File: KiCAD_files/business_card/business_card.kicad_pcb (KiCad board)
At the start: 2 copper layers, 88.9 x 50.8 mm, 114 parts, among them J2 Conn_01x05_Pin, Q1 AO3401A, SW1 CS1210F260, SW2 CS1210F260, SW3 CS1210F260, U1 STM32U073CCUx, U2 ST25DV04KC-IE6S3

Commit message: Add NFC Antenna
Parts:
- removed C2: 100nF, Capacitor_SMD:C_0603_1608Metric
- removed R10, R9: 10K, Resistor_SMD:R_0603_1608Metric
- added L1: 2.755 uH, Antenna:25X48MM_NFC, F.Cu at (164.4, 72.8)
- U2: value ST25DV04KC-IE6S3 -> ST25TN01K-AFH5; footprint ST25DV04KC-IE6S3:SO-8_STM -> ST25TN01K-AFH5:UFDFPN-5_1P8X1P5_STM
- moved G*** 57.5 mm to (120.2, 32.6)
- moved U2 9.94 mm to (147.2, 73.0), turned to 90 degrees
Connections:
- U1 pad 16: /NFC_SDA -> unconnected-(U1-PA6-Pad16)
- U1 pad 17: /NFC_SCL -> unconnected-(U1-PA7-Pad17)
- U2 pad 2: /L = 5.634 uH -> unconnected-(U2-NC-Pad2)
- U2 pad 3: /L = 5.634 uH -> Net-(U2-AC0)
- U2 pad 4: GND -> Net-(U2-AC1)
- U2 pad 5: /NFC_SDA -> unconnected-(U2-NC-Pad5)
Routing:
- net Net-(BT1-+): track 483.6 -> 11.7 mm
- net VDD: track 126.5 -> 105.1 mm, vias 4 -> 2
- net /NFC_SCL: track 12.4 -> 0.00 mm
- net /NFC_SDA: track 11.5 -> 0.00 mm, vias 2 -> 0
- net GND: track 101.3 -> 90.1 mm, vias 16 -> 14
- net Net-(U2-AC1): track 0.00 -> 7.45 mm, vias 0 -> 1
- net Net-(U2-AC0): track 0.00 -> 3.44 mm

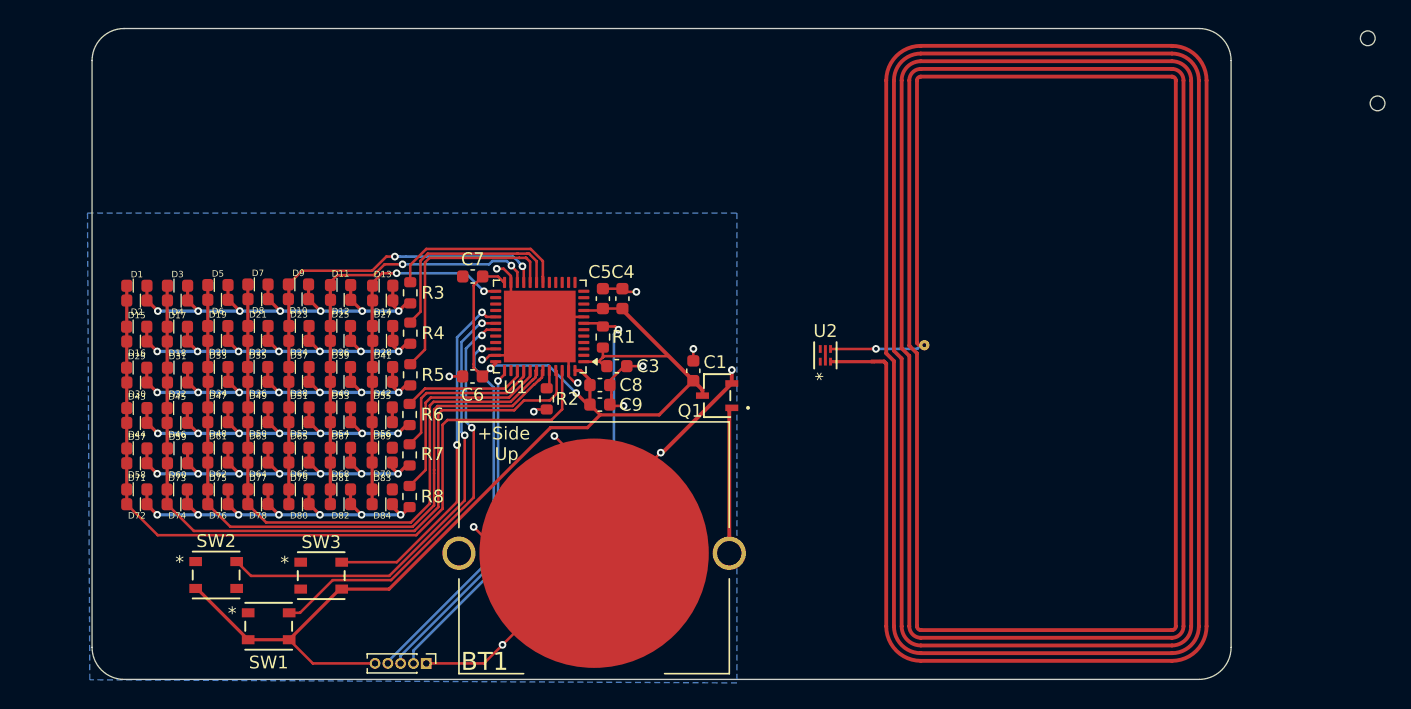
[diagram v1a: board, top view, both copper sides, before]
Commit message: Adjust LED Matrix Size
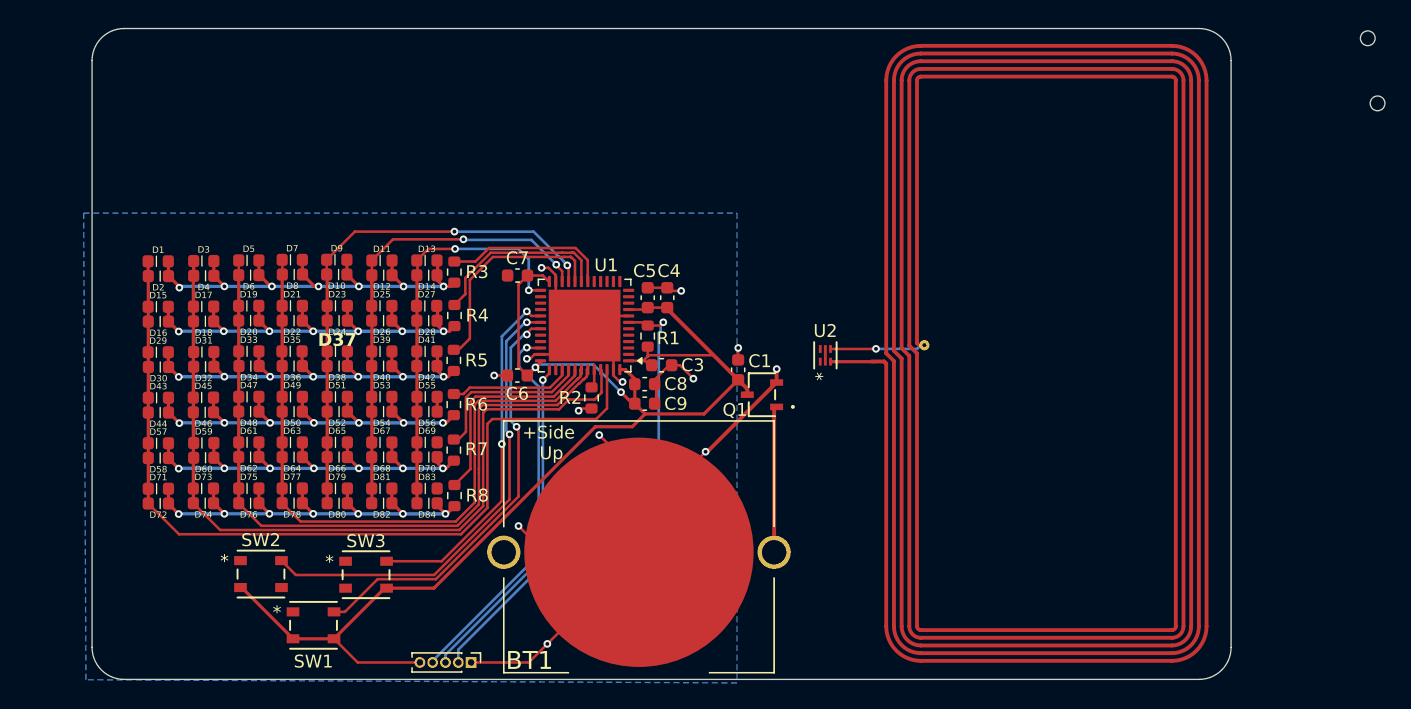
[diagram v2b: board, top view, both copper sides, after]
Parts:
- moved D13 3.97 mm to (116.0, 65.6)
- moved D14 3.97 mm to (116.0, 66.8)
- moved R3 3.80 mm to (118.2, 66.5)
- moved D27 3.78 mm to (116.0, 69.1)
- moved D28 3.78 mm to (116.0, 70.3)
- moved D11 3.76 mm to (112.5, 65.6)
- moved D12 3.76 mm to (112.5, 66.8)
- moved R4 3.71 mm to (118.2, 69.9)
- moved D41 3.67 mm to (116.0, 72.7)
- moved D42 3.67 mm to (116.0, 73.8)
- moved D55 3.60 mm to (116.1, 76.2)
- moved D56 3.60 mm to (116.1, 77.4)
- moved D25 3.59 mm to (112.5, 69.1)
- moved D26 3.59 mm to (112.5, 70.3)
- moved R5 3.58 mm to (118.2, 73.4)
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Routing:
- net /COL7: track 27.8 -> 32.1 mm
- net /COL1: track 63.0 -> 66.3 mm
- net /COL2: track 58.9 -> 62.0 mm
- net /COL5: track 38.2 -> 41.2 mm
- net /COL6: track 33.8 -> 36.6 mm
- net /COL3: track 53.7 -> 56.4 mm
- net /COL4: track 50.0 -> 52.4 mm
- net /ROW2: track 16.3 -> 14.2 mm
- net Net-(D1-A): track 36.6 -> 38.5 mm
- net Net-(D71-A): track 35.1 -> 36.9 mm
- net Net-(D43-A): track 35.4 -> 37.2 mm
- net Net-(D57-A): track 35.3 -> 37.0 mm
- net Net-(D15-A): track 36.1 -> 37.8 mm
- net /ROW3: track 18.5 -> 16.8 mm
- net Net-(D29-A): track 36.1 -> 37.8 mm
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
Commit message: Add Mouse Bites to Isolate Tooling Holes
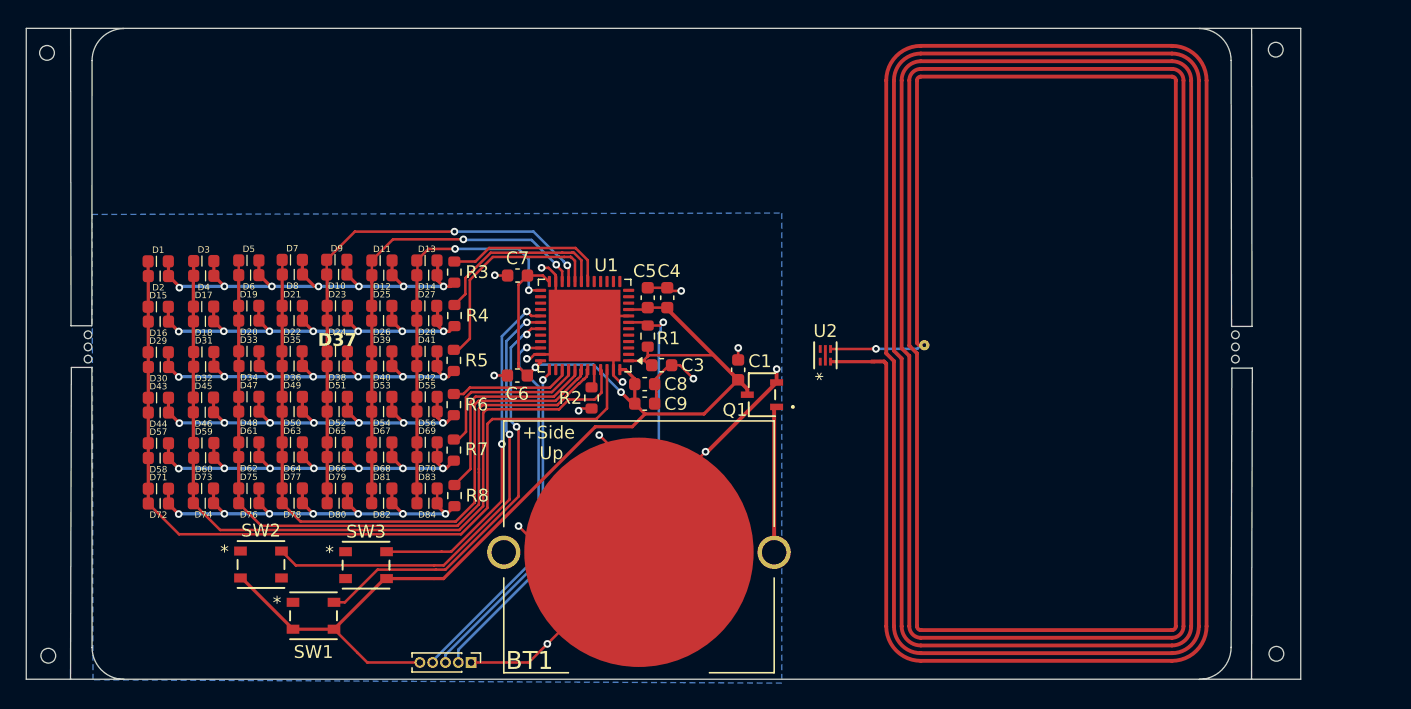
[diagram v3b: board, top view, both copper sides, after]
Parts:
- added H3: MountingHole, MountingHole:ToolingHole_1.152mm, F.Cu at (182.3, 49.1)
- added H4: MountingHole, MountingHole:ToolingHole_1.152mm, F.Cu at (86.5, 96.5)
- moved H2 103.1 mm to (86.4, 49.4)
- moved H1 43.7 mm to (182.3, 96.3)
- moved SW1 0.75 mm to (107.2, 93.3)
- moved SW2 0.75 mm to (103.1, 89.3)
- moved SW3 0.75 mm to (111.3, 89.4)
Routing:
- net Net-(D71-A): track 36.9 -> 38.0 mm
- net Net-(D57-A): track 37.0 -> 38.2 mm
- net Net-(D43-A): track 37.2 -> 38.3 mm
- net GND: track 90.0 -> 91.0 mm, vias 13 -> 14
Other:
- board size 88.9 x 50.8 mm -> 99.5 x 50.8 mm

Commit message: Move Components and Remove Unnecessary Silkscreen
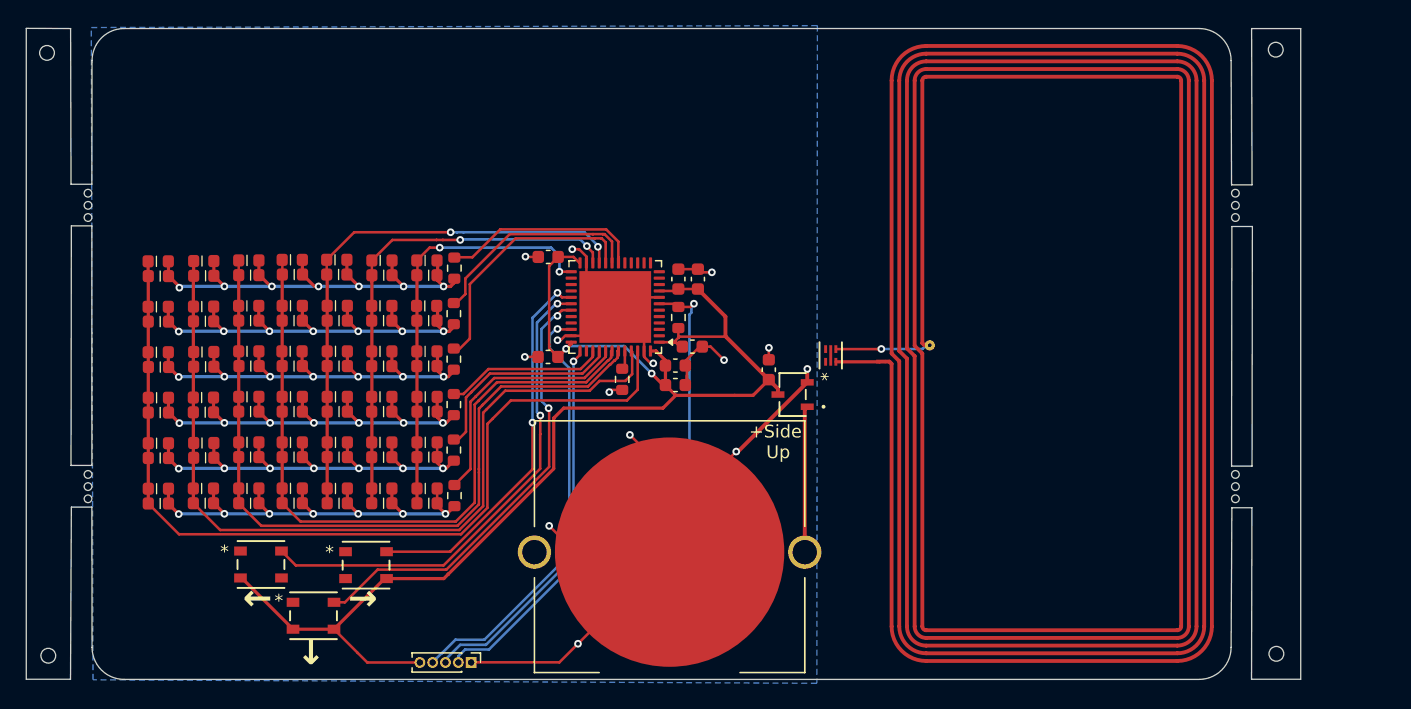
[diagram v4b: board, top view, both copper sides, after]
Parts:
- removed G***: LOGO, custom_footprints:qr_code
- moved C3 2.80 mm to (136.8, 72.3)
- moved C4 2.80 mm to (137.2, 67.1)
- moved C5 2.80 mm to (135.7, 67.1)
- moved C6 2.80 mm to (125.5, 73.1)
- moved C7 2.80 mm to (125.5, 65.3)
- moved C8 2.80 mm to (135.4, 73.8)
- moved C9 2.80 mm to (135.4, 75.3)
- moved R1 2.80 mm to (135.7, 70.1)
- moved R2 2.80 mm to (131.3, 74.9)
- moved U1 2.80 mm to (130.8, 69.2)
- moved C1 2.39 mm to (142.7, 74.1)
- moved Q1 2.39 mm to (144.6, 76.1)
- moved BT1 2.39 mm to (135.0, 88.4)
- moved L1 0.42 mm to (164.8, 72.9)
- moved U2 0.42 mm to (147.6, 73.0)
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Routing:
- net /SWDIO: track 30.0 -> 33.9 mm
- net /SWCLK: track 26.2 -> 29.8 mm
- net /NRST: track 36.1 -> 39.6 mm
- net /COL1: track 66.3 -> 69.3 mm
- net /ROW6: track 16.5 -> 19.5 mm
- net /ROW5: track 13.1 -> 16.0 mm
- net /COL3: track 56.4 -> 59.4 mm
- net /ROW4: track 9.51 -> 12.5 mm
- net /COL4: track 52.4 -> 55.4 mm
- net /COL2: track 62.0 -> 64.9 mm
- net /ROW2: track 14.2 -> 17.2 mm
- net /ROW1: track 12.9 -> 15.8 mm
- net /ROW3: track 16.8 -> 19.6 mm
- net /INPUT_DOWN: track 32.7 -> 35.2 mm
- net /INPUT_LEFT: track 36.1 -> 38.6 mm
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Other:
- outline, holes or cut-outs redrawn
- board text added: "←"
- board text added: "→"
- board text added: "↓"

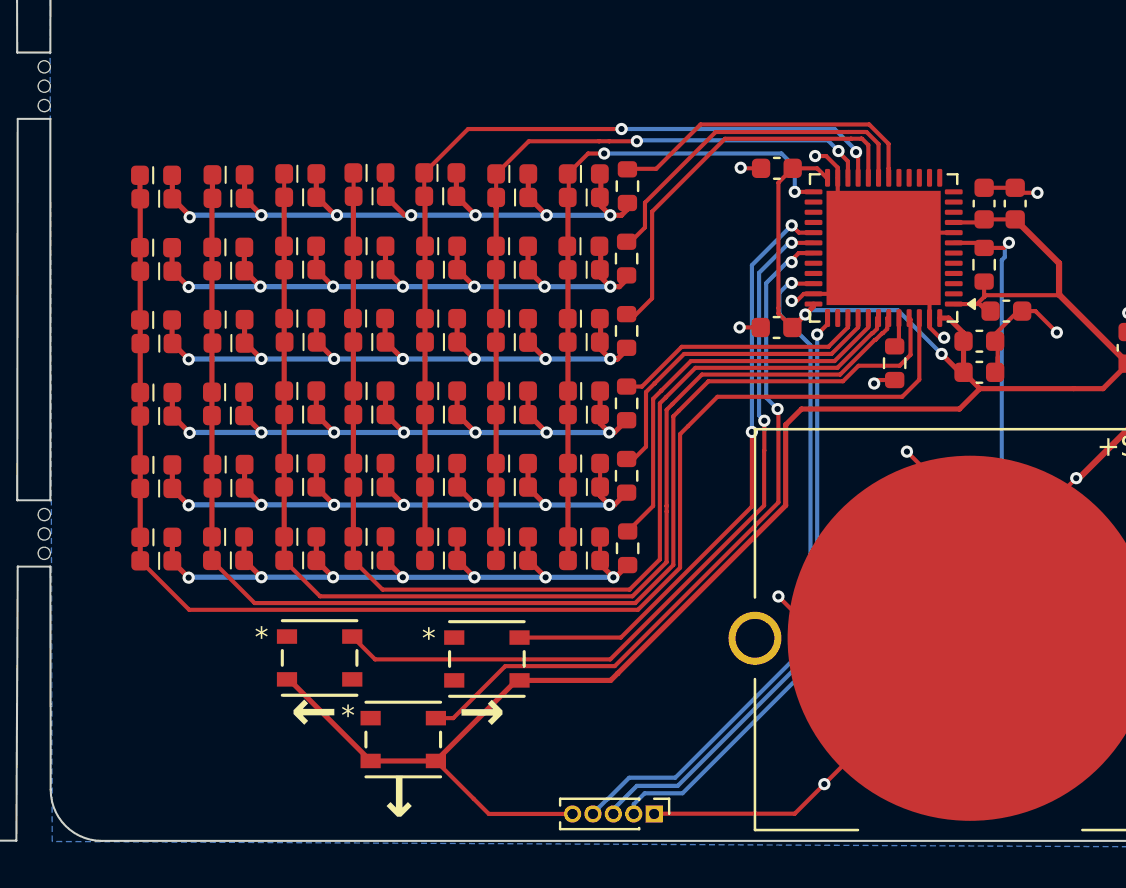
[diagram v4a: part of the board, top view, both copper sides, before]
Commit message: Change Debug Interface Connector Size
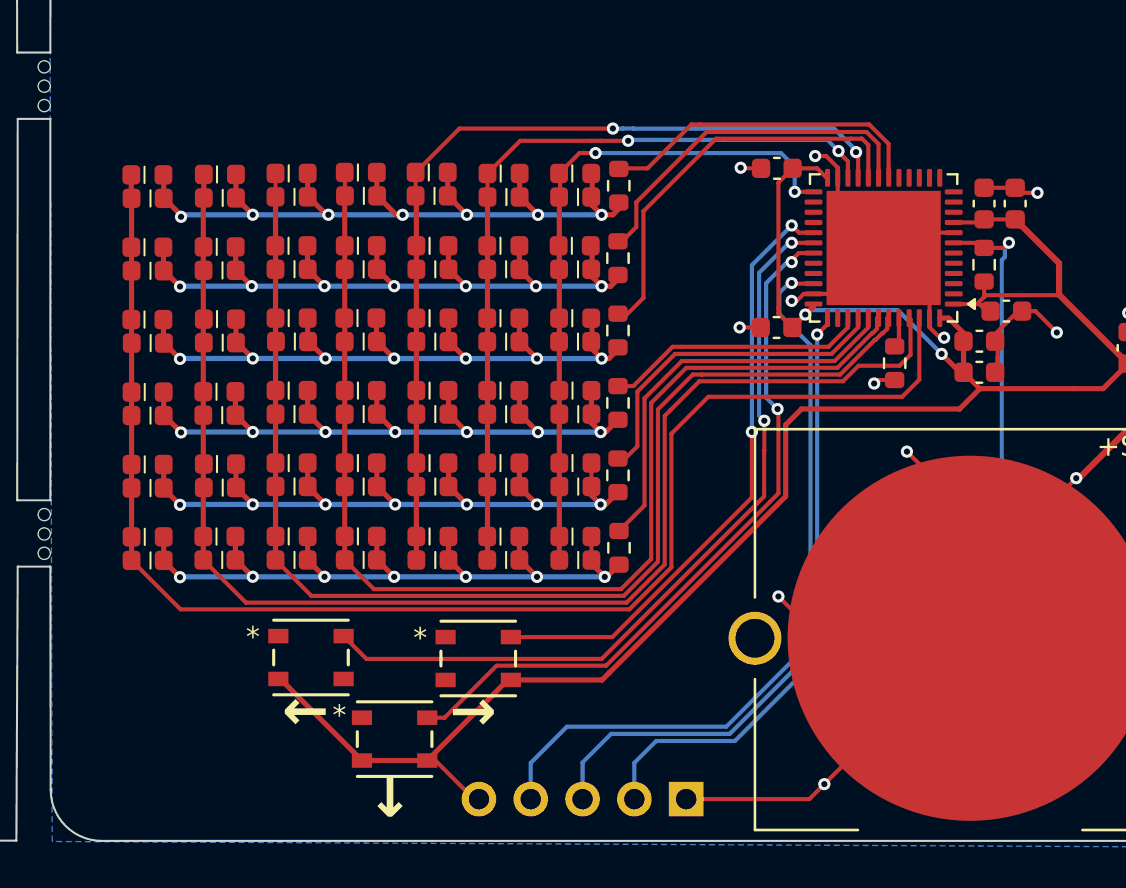
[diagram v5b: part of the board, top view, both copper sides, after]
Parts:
- J2: footprint Connector_PinHeader_1.00mm:PinHeader_1x05_P1.00mm_Vertical -> Connector_PinHeader_2.54mm:PinHeader_1x05_P2.54mm_Vertical
- moved J2 1.73 mm to (121.1, 96.2)
- moved D1 0.42 mm to (94.7, 65.6)
- moved D12 0.42 mm to (112.1, 66.7)
- moved D14 0.42 mm to (115.6, 66.7)
- moved D16 0.42 mm to (94.7, 70.3)
- moved D19 0.42 mm to (101.7, 69.1)
- moved D20 0.42 mm to (101.7, 70.3)
- moved D21 0.42 mm to (105.1, 69.1)
- moved D23 0.42 mm to (108.6, 69.1)
- moved D25 0.42 mm to (112.1, 69.1)
- moved D26 0.42 mm to (112.1, 70.3)
- moved D27 0.42 mm to (115.6, 69.1)
- moved D28 0.42 mm to (115.6, 70.3)
- moved D29 0.42 mm to (94.7, 72.7)
- moved D3 0.42 mm to (98.2, 65.6)
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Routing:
- net VDD: track 107.2 -> 102.2 mm
- net /SWDIO: track 33.9 -> 37.6 mm
- net /SWCLK: track 29.8 -> 32.0 mm
- net GND: track 93.4 -> 91.5 mm
